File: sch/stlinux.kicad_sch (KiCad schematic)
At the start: 0 parts

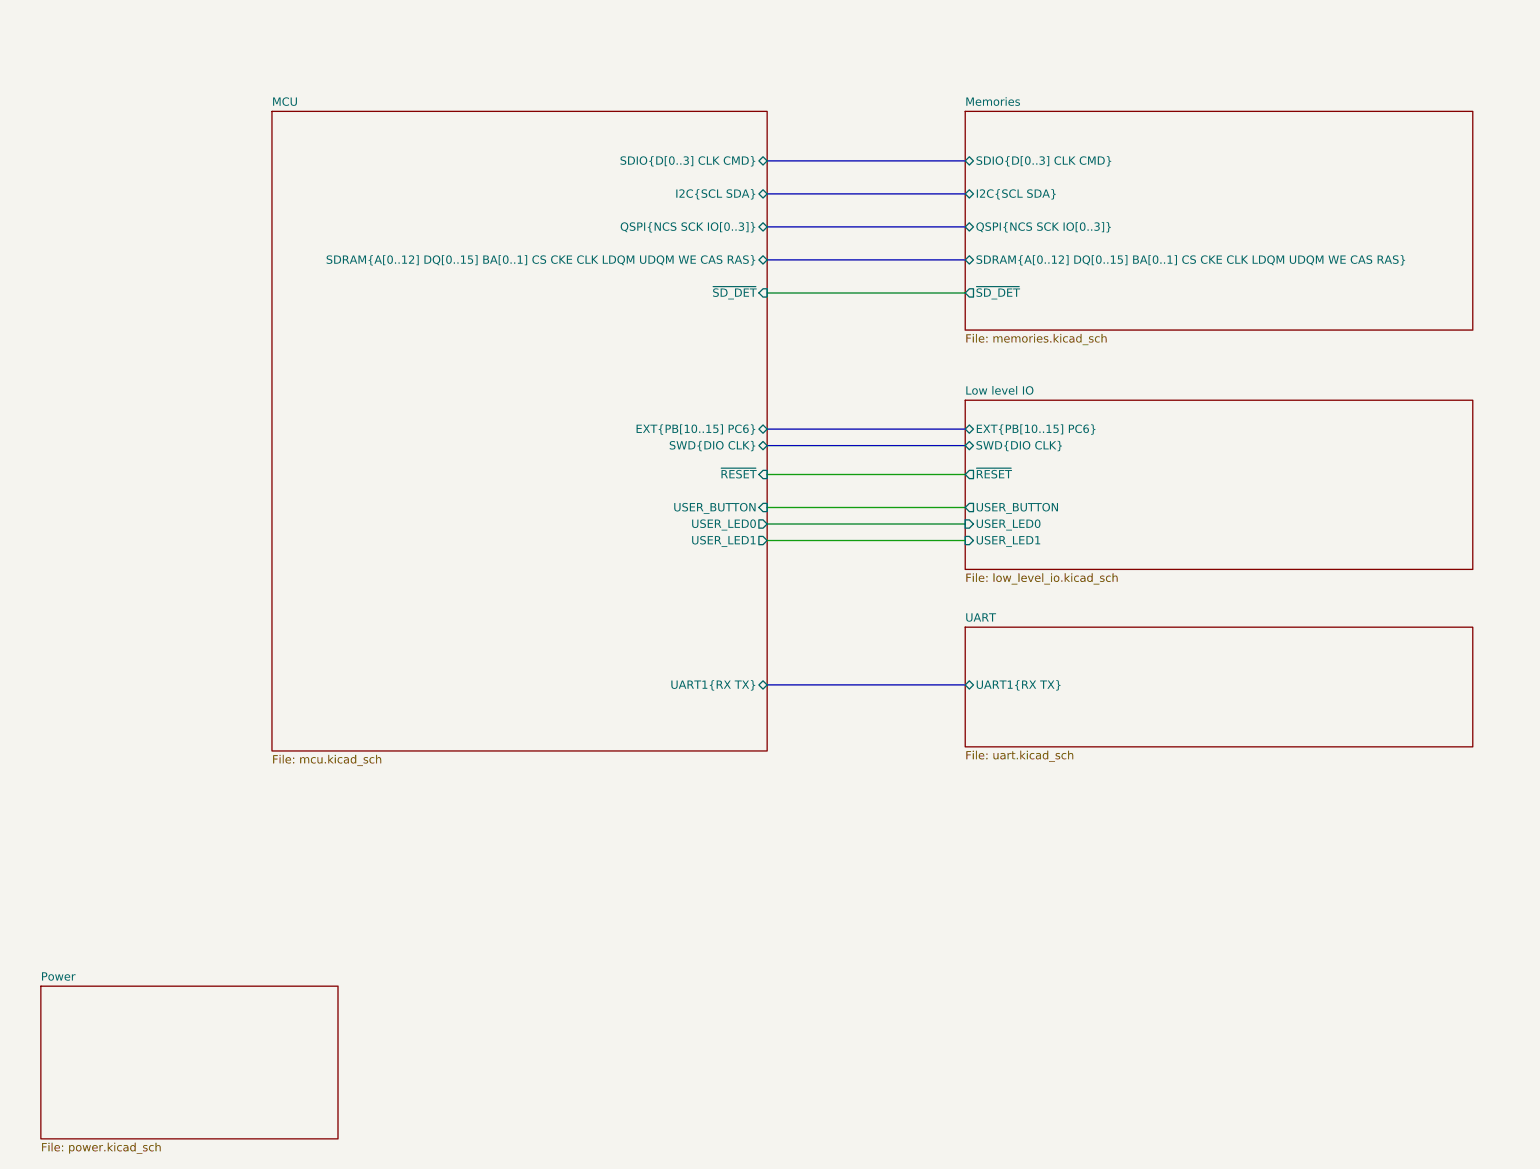
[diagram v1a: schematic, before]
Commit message: Added more expansion capability.
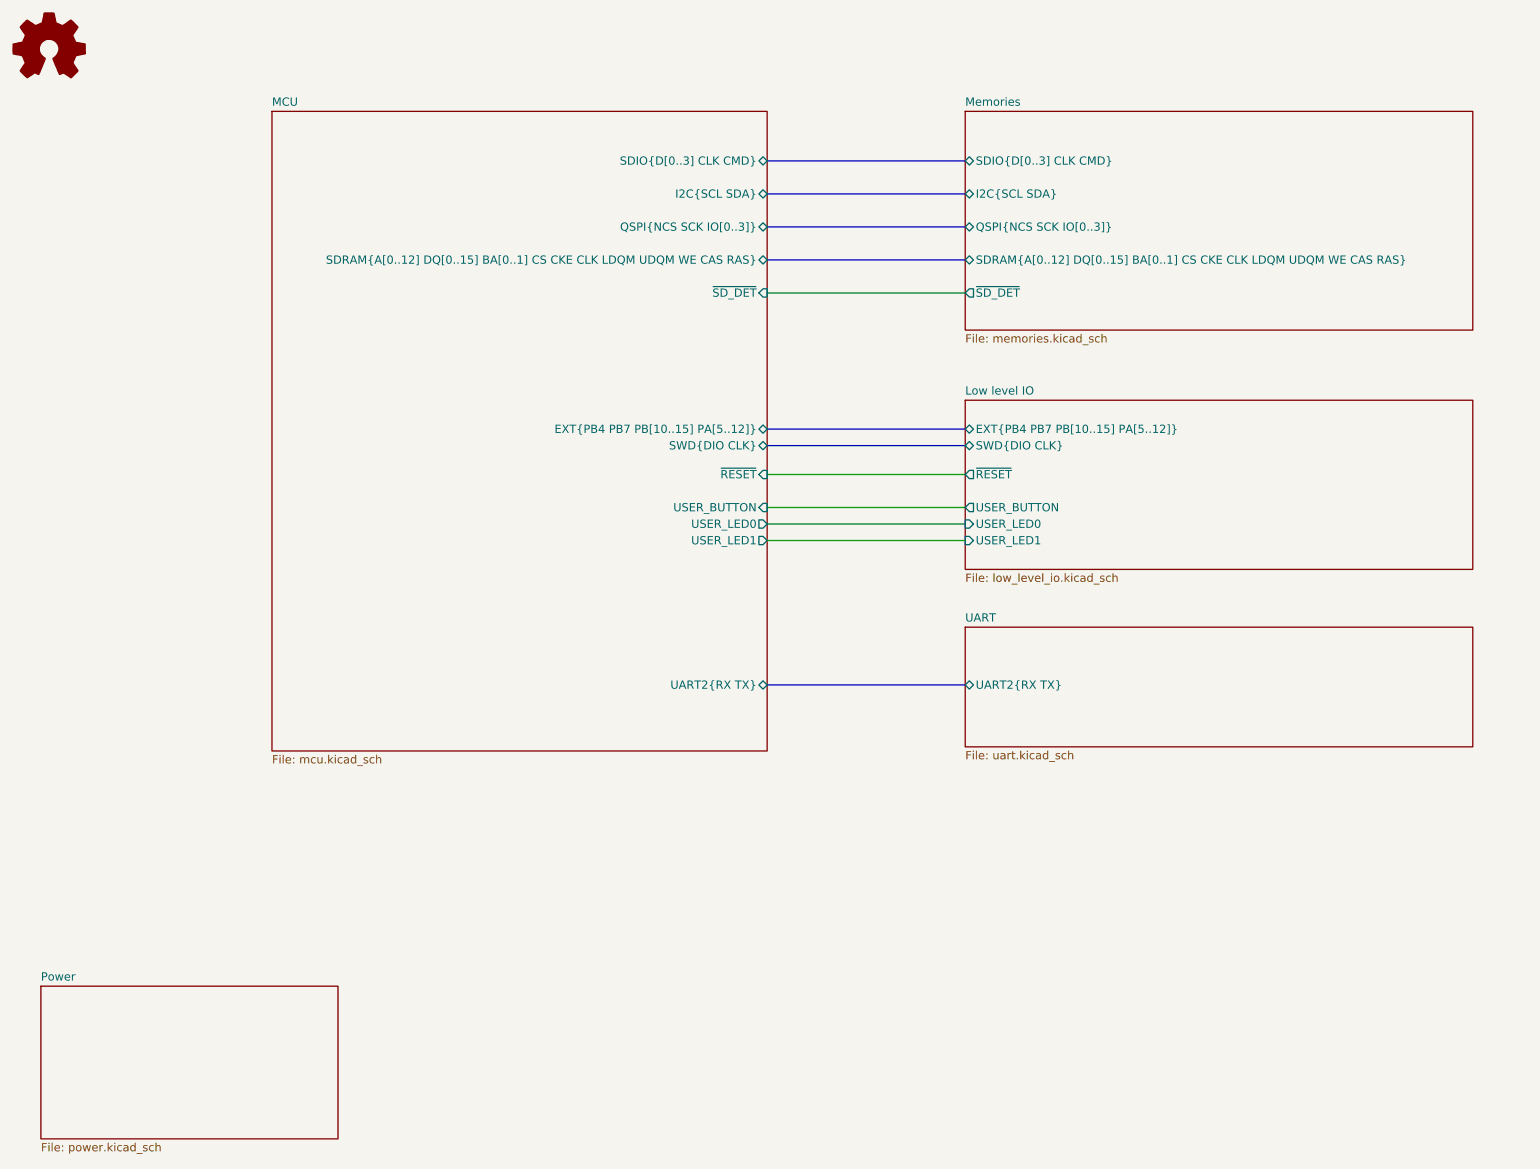
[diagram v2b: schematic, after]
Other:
- sheet Low level IO ports: added EXT{PB4 PB7 PB[10..15] PA[5..12]}; removed EXT{PB[10..15] PC6}
- sheet MCU ports: added EXT{PB4 PB7 PB[10..15] PA[5..12]}, UART2{RX TX}; removed EXT{PB[10..15] PC6}, UART1{RX TX}
- sheet UART ports: added UART2{RX TX}; removed UART1{RX TX}
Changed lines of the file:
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@@
     (stroke (width 0) (type default) (color 0 0 0 0))
+  )
+  (symbol (lib_id "Graphic:Logo_Open_Hardware_Small") (at 20.955 20.955 0) (unit 1)
+    (in_bom yes) (on_board yes) (fields_autoplaced)
+    (property "Reference" "#LOGO101" (id 0) (at 20.955 13.97 0)
+      (effects (font (size 1.27 1.27)) hide)
+    )
+    (property "Value" "Logo_Open_Hardware_Small" (id 1) (at 20.955 26.67 0)
+      (effects (font (size 1.27 1.27)) hide)
+    )
+    (property "Footprint" "Symbol:OSHW-Logo_5.7x6mm_SilkScreen" (id 2) (at 20.955 20.955 0)
+      (effects (font (size 1.27 1.27)) hide)
+    )
+    (property "Datasheet" "~" (id 3) (at 20.955 20.955 0)
+      (effects (font (size 1.27 1.27)) hide)
+    )
   )
   (sheet (at 161.925 74.93) (size 78.105 26.035) (fields_autoplaced)
@@
       (effects (font (size 1.27 1.27)) (justify left))
     )
-    (pin "EXT{PB[10..15] PC6}" bidirectional (at 161.925 79.375 180)
+    (pin "EXT{PB4 PB7 PB[10..15] PA[5..12]}" bidirectional (at 161.925 79.375 180)
       (effects (font (size 1.27 1.27)) (justify left))
     )
@@
       (effects (font (size 1.27 1.27)) (justify left top))
     )
-    (pin "UART1{RX TX}" bidirectional (at 161.925 118.745 180)
+    (pin "UART2{RX TX}" bidirectional (at 161.925 118.745 180)
       (effects (font (size 1.27 1.27)) (justify left))
     )
@@
       (effects (font (size 1.27 1.27)) (justify right))
     )
-    (pin "UART1{RX TX}" bidirectional (at 131.445 118.745 0)
+    (pin "UART2{RX TX}" bidirectional (at 131.445 118.745 0)
       (effects (font (size 1.27 1.27)) (justify right))
     )
@@
       (effects (font (size 1.27 1.27)) (justify right))
     )
-    (pin "EXT{PB[10..15] PC6}" bidirectional (at 131.445 79.375 0)
+    (pin "EXT{PB4 PB7 PB[10..15] PA[5..12]}" bidirectional (at 131.445 79.375 0)
       (effects (font (size 1.27 1.27)) (justify right))
     )
@@
   )
   (symbol_instances
+    (path "/4d92554c-5d68-480f-910f-ef1b667a13ea"
+      (reference "#LOGO101") (unit 1) (value "Logo_Open_Hardware_Small") (footprint "Symbol:OSHW-Logo_5.7x6mm_SilkScreen")
+    )
     (path "/8d833852-dfc1-4f20-b1c5-73dd83c6a430/c0221383-dd2b-46f7-8e5f-23508101ae7f"
       (reference "#PWR0201") (unit 1) (value "VDD") (footprint "")
@@
       (reference "#PWR0401") (unit 1) (value "VDD") (footprint "")
     )
+    (path "/1d765368-b231-4dd8-81c4-02b8a42d5091/dcd50c57-ccf4-4a67-af2f-917ecac95fe2"
+      (reference "#PWR0402") (unit 1) (value "GND") (footprint "")
+    )
+    (path "/1d765368-b231-4dd8-81c4-02b8a42d5091/ba9013c3-bc87-4ab2-98c6-946d587d2f22"
+      (reference "#PWR0403") (unit 1) (value "VDD") (footprint "")
+    )
+    (path "/1d765368-b231-4dd8-81c4-02b8a42d5091/f5a45c34-1954-4e59-8924-26cbb83b50fb"
+      (reference "#PWR0404") (unit 1) (value "+5V") (footprint "")
+    )
     (path "/1d765368-b231-4dd8-81c4-02b8a42d5091/70a0a714-958c-485a-bc73-ecaa1f60dfaf"
-      (reference "#PWR0402") (unit 1) (value "GND") (footprint "")
+      (reference "#PWR0405") (unit 1) (value "GND") (footprint "")
     )
     (path "/1d765368-b231-4dd8-81c4-02b8a42d5091/619d80dc-7386-465d-af83-cf06335e373b"
-      (reference "#PWR0403") (unit 1) (value "VDD") (footprint "")
+      (reference "#PWR0406") (unit 1) (value "VDD") (footprint "")
     )
     (path "/1d765368-b231-4dd8-81c4-02b8a42d5091/5203b50e-52cf-4cc6-881d-ef640e961c6c"
-      (reference "#PWR0404") (unit 1) (value "+5V") (footprint "")
+      (reference "#PWR0407") (unit 1) (value "+5V") (footprint "")
     )
     (path "/1d765368-b231-4dd8-81c4-02b8a42d5091/7a292660-0299-406b-94c3-c397a4fc6998"
-      (reference "#PWR0405") (unit 1) (value "GND") (footprint "")
+      (reference "#PWR0408") (unit 1) (value "GND") (footprint "")
     )
     (path "/1d765368-b231-4dd8-81c4-02b8a42d5091/85959436-d56a-4a41-ae88-4eae5437c502"
-      (reference "#PWR0406") (unit 1) (value "VDD") (footprint "")
+      (reference "#PWR0409") (unit 1) (value "VDD") (footprint "")
     )
     (path "/1d765368-b231-4dd8-81c4-02b8a42d5091/86d17215-8ce5-43b4-8838-5ab53049c68d"
-      (reference "#PWR0407") (unit 1) (value "GND") (footprint "")
+      (reference "#PWR0410") (unit 1) (value "GND") (footprint "")
     )
     (path "/1d765368-b231-4dd8-81c4-02b8a42d5091/aaf29199-a13f-42ec-94bf-0caf44baf3a5"
-      (reference "#PWR0408") (unit 1) (value "VDD") (footprint "")
+      (reference "#PWR0411") (unit 1) (value "VDD") (footprint "")
     )
     (path "/1d765368-b231-4dd8-81c4-02b8a42d5091/2b3c35aa-c352-44a3-ada9-f38a05c3c4fc"
-      (reference "#PWR0409") (unit 1) (value "VDD") (footprint "")
+      (reference "#PWR0412") (unit 1) (value "VDD") (footprint "")
     )
     (path "/1d765368-b231-4dd8-81c4-02b8a42d5091/58a84299-0203-4144-be68-71785d4b904d"
-      (reference "#PWR0410") (unit 1) (value "VDD") (footprint "")
+      (reference "#PWR0413") (unit 1) (value "VDD") (footprint "")
     )
     (path "/618836ab-4af1-4f80-b77c-329df8a9683b/24a0e5be-5808-4c8a-ab6d-da1a444987ae"
@@
     )
     (path "/1d765368-b231-4dd8-81c4-02b8a42d5091/2eadc4cd-1dcf-4b95-9730-37250ecad8f8"
-      (reference "J401") (unit 1) (value "Extension") (footprint "Connector_PinSocket_2.54mm:PinSocket_2x06_P2.54mm_Vertical")
+      (reference "J401") (unit 1) (value "Extension") (footprint "Connector_PinSocket_2.54mm:PinSocket_2x06_P2.54mm_Vertical_SMD")
+    )
+    (path "/1d765368-b231-4dd8-81c4-02b8a42d5091/770e1af7-abe4-4f50-9e07-aaeeeeda7425"
+      (reference "J402") (unit 1) (value "Extension") (footprint "Connector_PinSocket_2.54mm:PinSocket_2x06_P2.54mm_Vertical_SMD")
     )
     (path "/618836ab-4af1-4f80-b77c-329df8a9683b/8e76d0be-289e-4fb4-baa6-058dd6901042"
@@
     )
     (path "/5f4c6225-c840-4642-8672-7da53c591482/b46338e1-ca1a-4253-b8ae-d55845efd2d0"
-      (reference "U303") (unit 1) (value "IS42S16160B-7TL") (footprint "Package_SO:TSOP-II-54_22.2x10.16mm_P0.8mm")
+      (reference "U303") (unit 1) (value "IS42S16160J") (footprint "Package_SO:TSOP-II-54_22.2x10.16mm_P0.8mm")
     )
     (path "/618836ab-4af1-4f80-b77c-329df8a9683b/dc90786b-82f1-4bdc-aec6-60bad1110fa9"
